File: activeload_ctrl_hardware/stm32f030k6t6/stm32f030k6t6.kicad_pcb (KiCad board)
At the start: 2 copper layers, 98 x 85 mm, 45 parts, among them J1 Supply, J2 LCD, J3 SWD, J4 USART, J5 Module, J6 Supply, SW2 SW_Push, SW3 SW_Push, SW4 SW_Push, U1 STM32F030K6Tx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

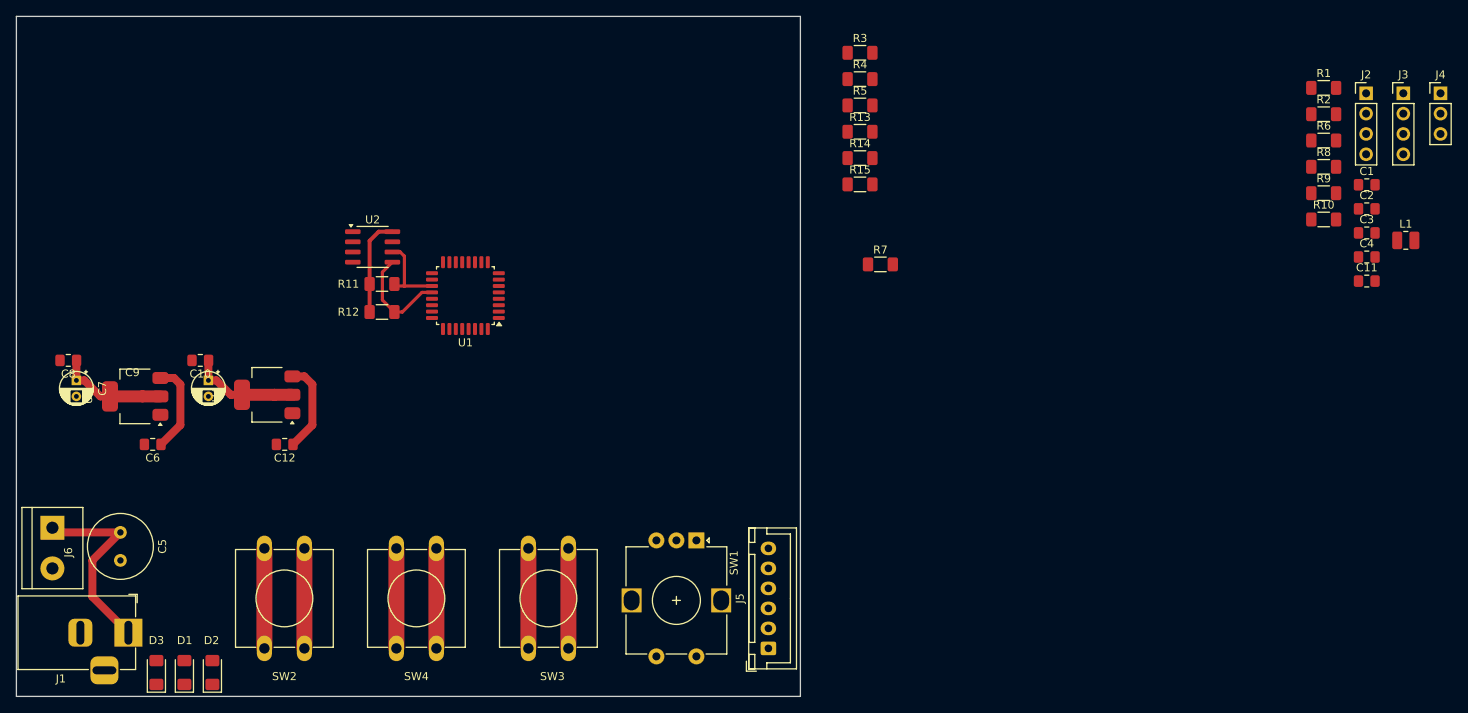
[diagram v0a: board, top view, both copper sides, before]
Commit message: stm32f030k6t6 pcb
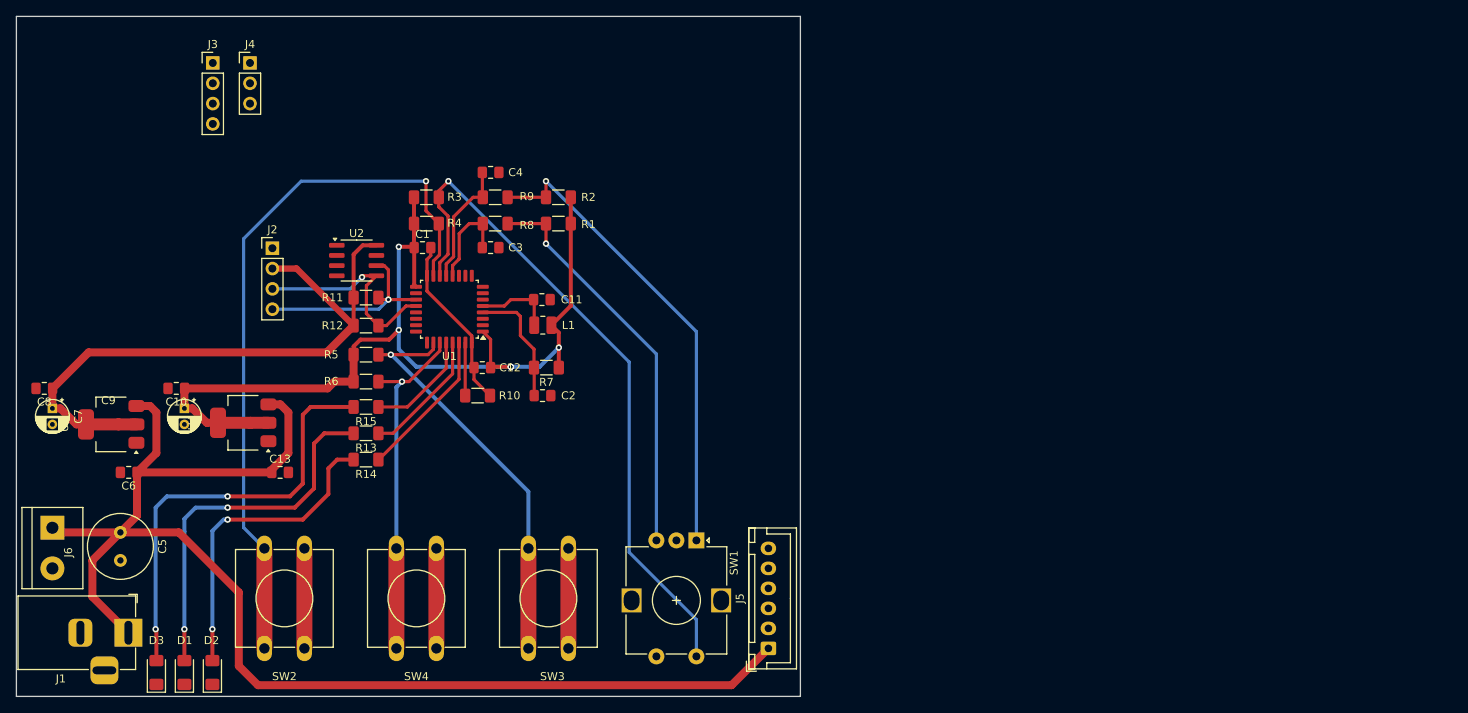
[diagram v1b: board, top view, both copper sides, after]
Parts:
- added C13: 0.1u, Capacitor_SMD:C_0805_2012Metric_Pad1.18x1.45mm_HandSolder, F.Cu at (183.0, 97.0)
- moved J3 148.9 mm to (174.6, 45.8)
- moved J4 148.9 mm to (179.2, 45.8)
- moved J2 138.1 mm to (182.0, 69.0)
- moved R6 123.4 mm to (193.7, 85.7)
- moved C1 118.3 mm to (200.8, 68.9)
- moved C4 110.0 mm to (209.3, 59.5)
- moved C3 109.5 mm to (209.3, 68.9)
- moved L1 108.4 mm to (215.8, 78.6), turned to 180 degrees
- moved R10 108.0 mm to (207.7, 87.4)
- moved C2 105.6 mm to (215.8, 87.4)
- moved R8 103.8 mm to (209.8, 65.9), turned to 180 degrees
- moved R9 103.6 mm to (209.8, 62.6), turned to 180 degrees
- moved C11 103.1 mm to (215.7, 75.4)
- moved R1 96.6 mm to (217.8, 65.9), turned to 180 degrees
- moved R2 96.6 mm to (217.8, 62.6), turned to 180 degrees
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- renumbered R2 to R1, R14 to R13, R15 to R14, R13 to R15, R1 to R2
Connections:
- C3 pad 1: /ENC_A -> /ENC1
- C4 pad 1: /ENC_B -> /ENC2
- R1 pad 2: Net-(R2-Pad2) -> Net-(R1-Pad2)
- R13 pad 1: /LED_R -> /LED_G
- R13 pad 2: Net-(D2-A) -> Net-(D1-A)
- R14 pad 1: /LED_Y -> /LED_R
- R14 pad 2: Net-(D3-A) -> Net-(D2-A)
- R15 pad 1: /LED_G -> /LED_Y
- R15 pad 2: Net-(D1-A) -> Net-(D3-A)
- R2 pad 2: Net-(R1-Pad2) -> Net-(R2-Pad2)
- R8 pad 2: /ENC_A -> /ENC1
- R9 pad 2: /ENC_B -> /ENC2
- SW1 pad A: Net-(R1-Pad2) -> Net-(R2-Pad2)
- SW1 pad B: Net-(R2-Pad2) -> Net-(R1-Pad2)
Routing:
- net +12V: track 47.4 -> 168.4 mm
- net +3.3V: track 13.8 -> 124.2 mm, vias 0 -> 5
- net /ENC_BTN: track 0.00 -> 85.5 mm, vias 0 -> 1
- net /BTN1: track 12.5 -> 90.9 mm, vias 0 -> 1
- net Net-(R2-Pad2): track 0.00 -> 59.5 mm, vias 0 -> 1
- net Net-(D3-A): track 0.00 -> 54.2 mm, vias 0 -> 2
- net +5V: track 26.1 -> 80.0 mm
- net Net-(R1-Pad2): track 0.00 -> 50.1 mm, vias 0 -> 1
- net Net-(D1-A): track 0.00 -> 46.6 mm, vias 0 -> 2
- net Net-(D2-A): track 0.00 -> 39.4 mm, vias 0 -> 2
- net /BTN2: track 12.5 -> 51.9 mm, vias 0 -> 1
- net /BTN3: track 12.5 -> 43.9 mm, vias 0 -> 1
- net GND: track 37.5 -> 59.5 mm
- net /LED_R: track 0.00 -> 18.8 mm
- net /LED_G: track 0.00 -> 16.3 mm
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
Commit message: stm32f030k6t6 pcb in grogress
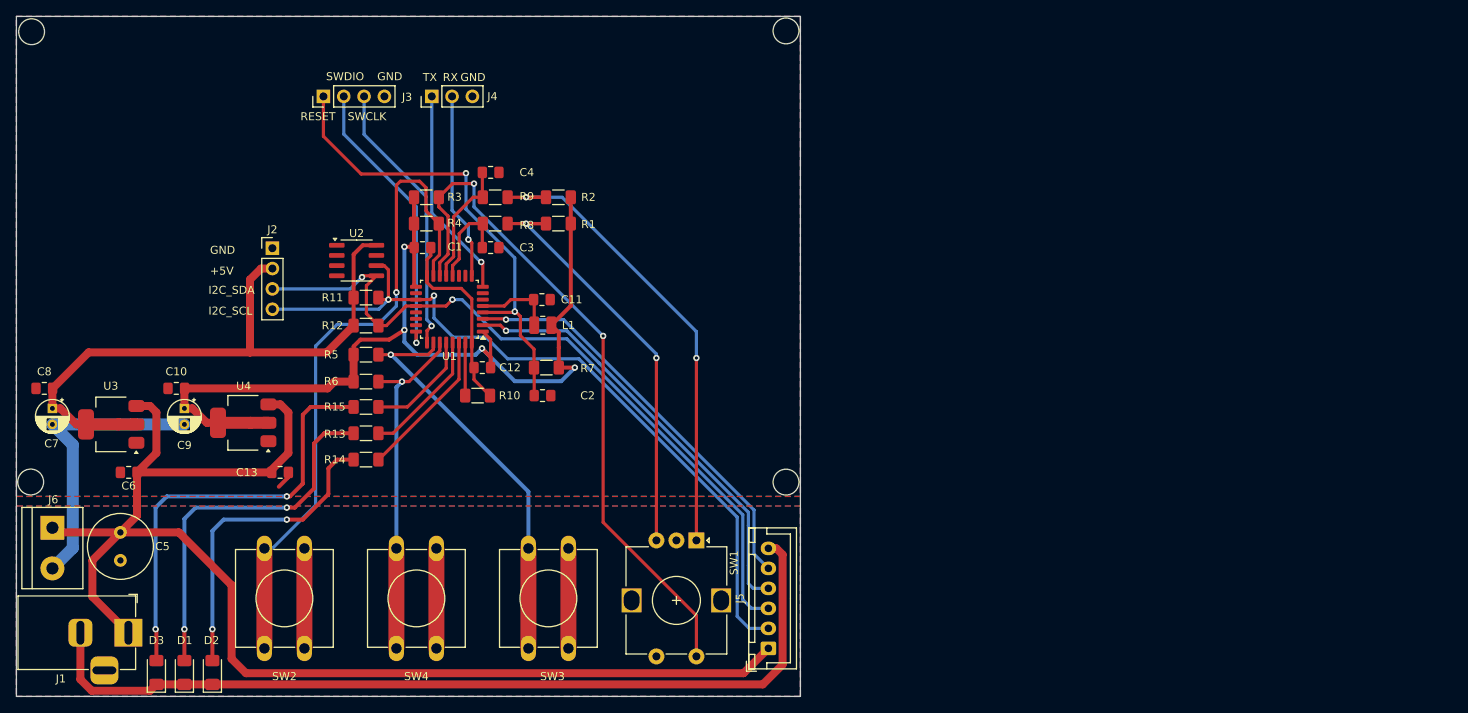
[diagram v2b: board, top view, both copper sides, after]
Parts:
- moved J4 23.1 mm to (201.9, 50.0), turned to 90 degrees
- moved J3 14.4 mm to (188.4, 50.0), turned to 90 degrees
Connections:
- U1 pad 12: /ENC_A -> /ENC1
- U1 pad 13: /ENC_B -> /ENC2
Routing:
- net GND: track 59.5 -> 211.8 mm
- net /I2C_SCL: track 25.3 -> 95.7 mm, vias 1 -> 2
- net /I2C_SDA: track 26.8 -> 93.4 mm, vias 1 -> 2
- net /~{WOE}: track 0.00 -> 54.5 mm, vias 0 -> 1
- net /WOE: track 0.00 -> 51.8 mm, vias 0 -> 1
- net /RESET: track 15.5 -> 60.2 mm, vias 0 -> 2
- net /SWDIO: track 0.00 -> 36.0 mm, vias 0 -> 1
- net /SWCLK: track 0.00 -> 34.5 mm, vias 0 -> 1
- net /USART_TX: track 0.00 -> 26.5 mm, vias 0 -> 1
- net /USART_RX: track 0.00 -> 23.4 mm, vias 0 -> 1
- net /ENC_B: track 15.6 -> 0.00 mm
- net /ENC2: track 0.00 -> 15.6 mm
- net /ENC1: track 0.00 -> 12.2 mm
- net /ENC_A: track 12.1 -> 0.00 mm
- net /BTN1: track 90.9 -> 84.6 mm
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- added copper zone on B.Cu, net GND
- added copper zone on F.Cu, net GND
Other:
- outline, holes or cut-outs redrawn
- board text added: "+5V"
- board text added: "GND"
- board text added: "I2C_SCL"
- board text added: "I2C_SDA"
- board text added: "RESET"
- board text added: "RX"
- board text added: "SWCLK"
- board text added: "SWDIO"
- board text added: "TX"
